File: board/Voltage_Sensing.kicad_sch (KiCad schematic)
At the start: 40 parts, among them U4 Opamp_Dual, U5 Opamp_Dual, U6 Opamp_Dual

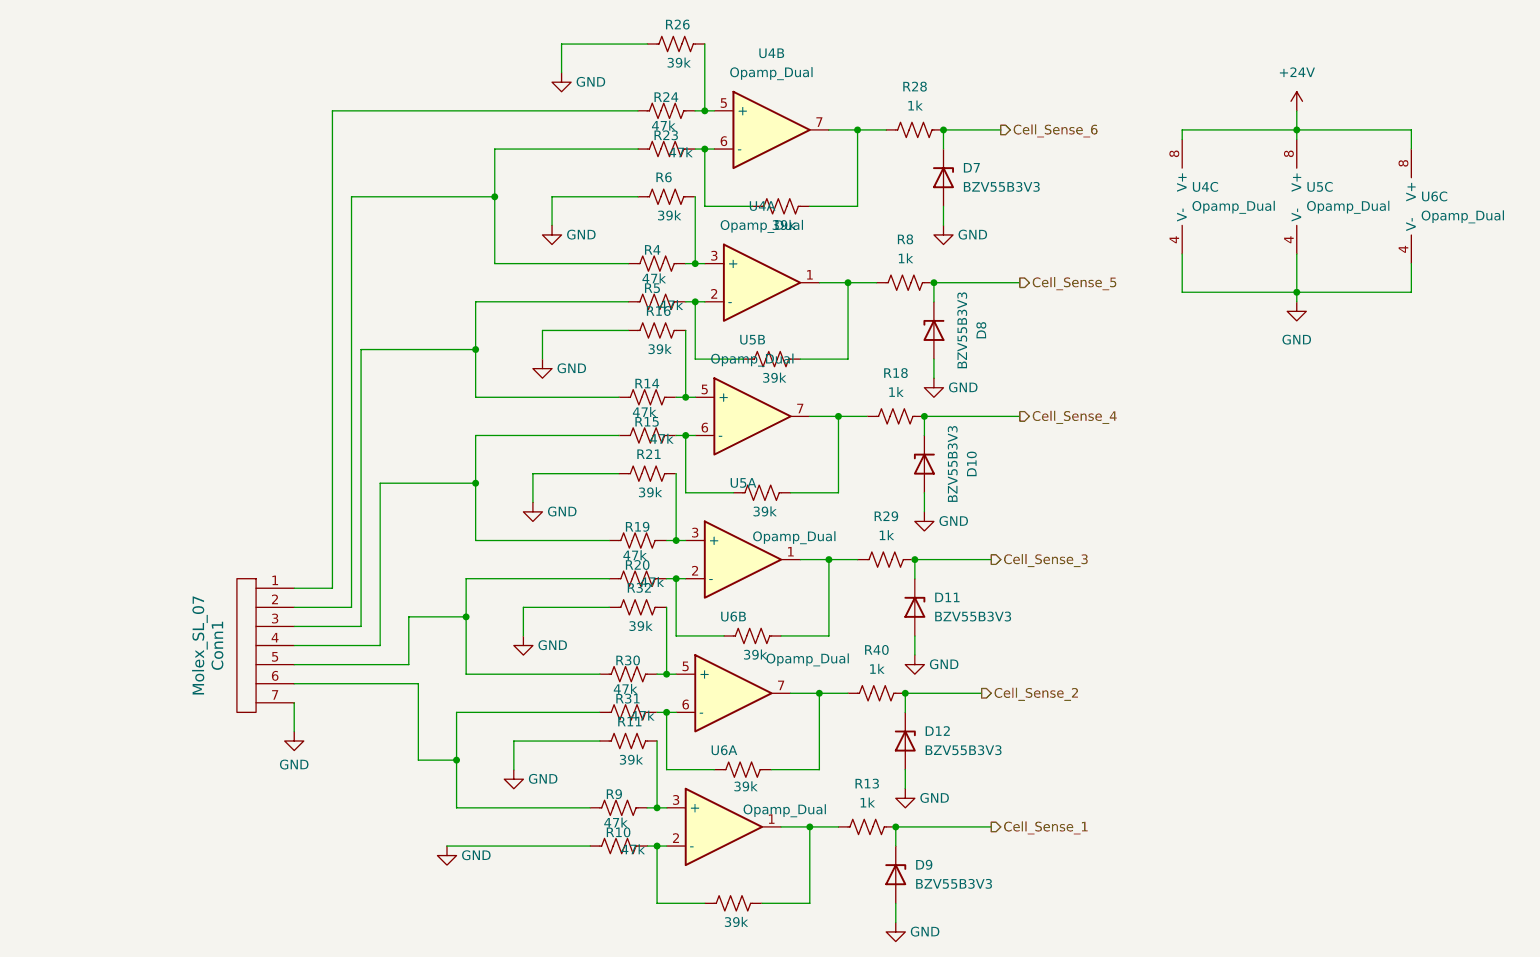
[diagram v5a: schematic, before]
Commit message: Center schematics and layout for prettiness
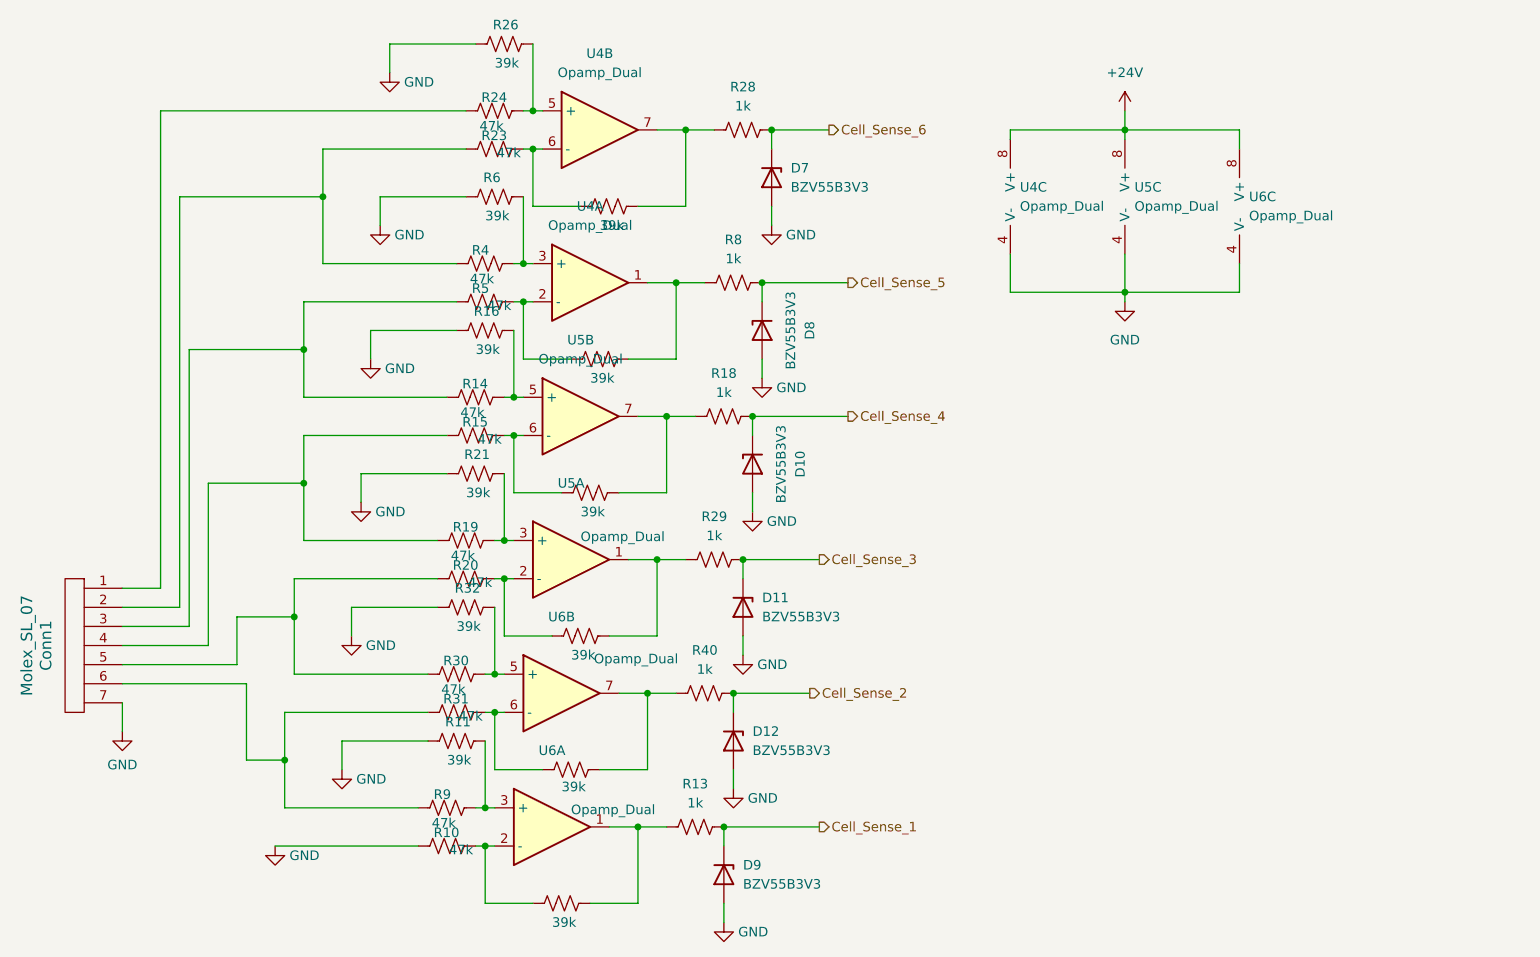
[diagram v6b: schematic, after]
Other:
- moved on the sheet: Conn1, D10, D11, D12, D7, D8, D9, R10, R11, R13, R14, R15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

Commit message: clean up board a tiny bit
this took way too long
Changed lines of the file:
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@@
 		(on_board yes)
 		(dnp no)
-		(fields_autoplaced yes)
 		(property "Reference" "U5"
 			(at 132.08 64.77 0)
@@
 		)
 		(property "Value" "Opamp_Dual"
-			(at 132.08 67.31 0)
+			(at 140.462 71.628 0)
 			(effects
 				(font

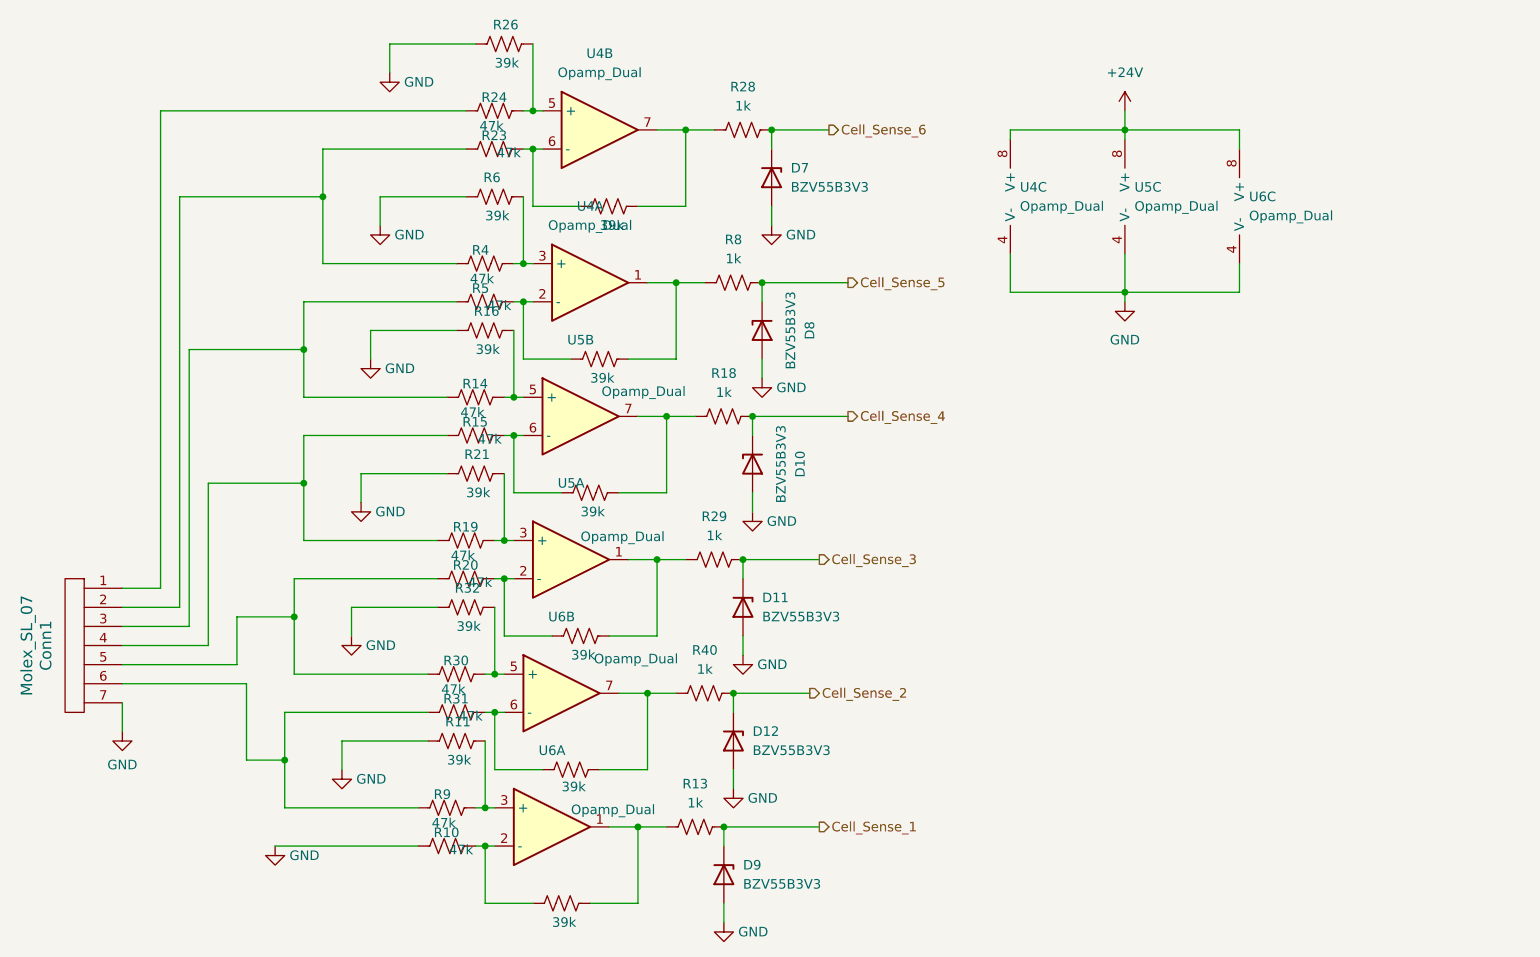
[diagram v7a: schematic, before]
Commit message: add label for battery sensing molex connector
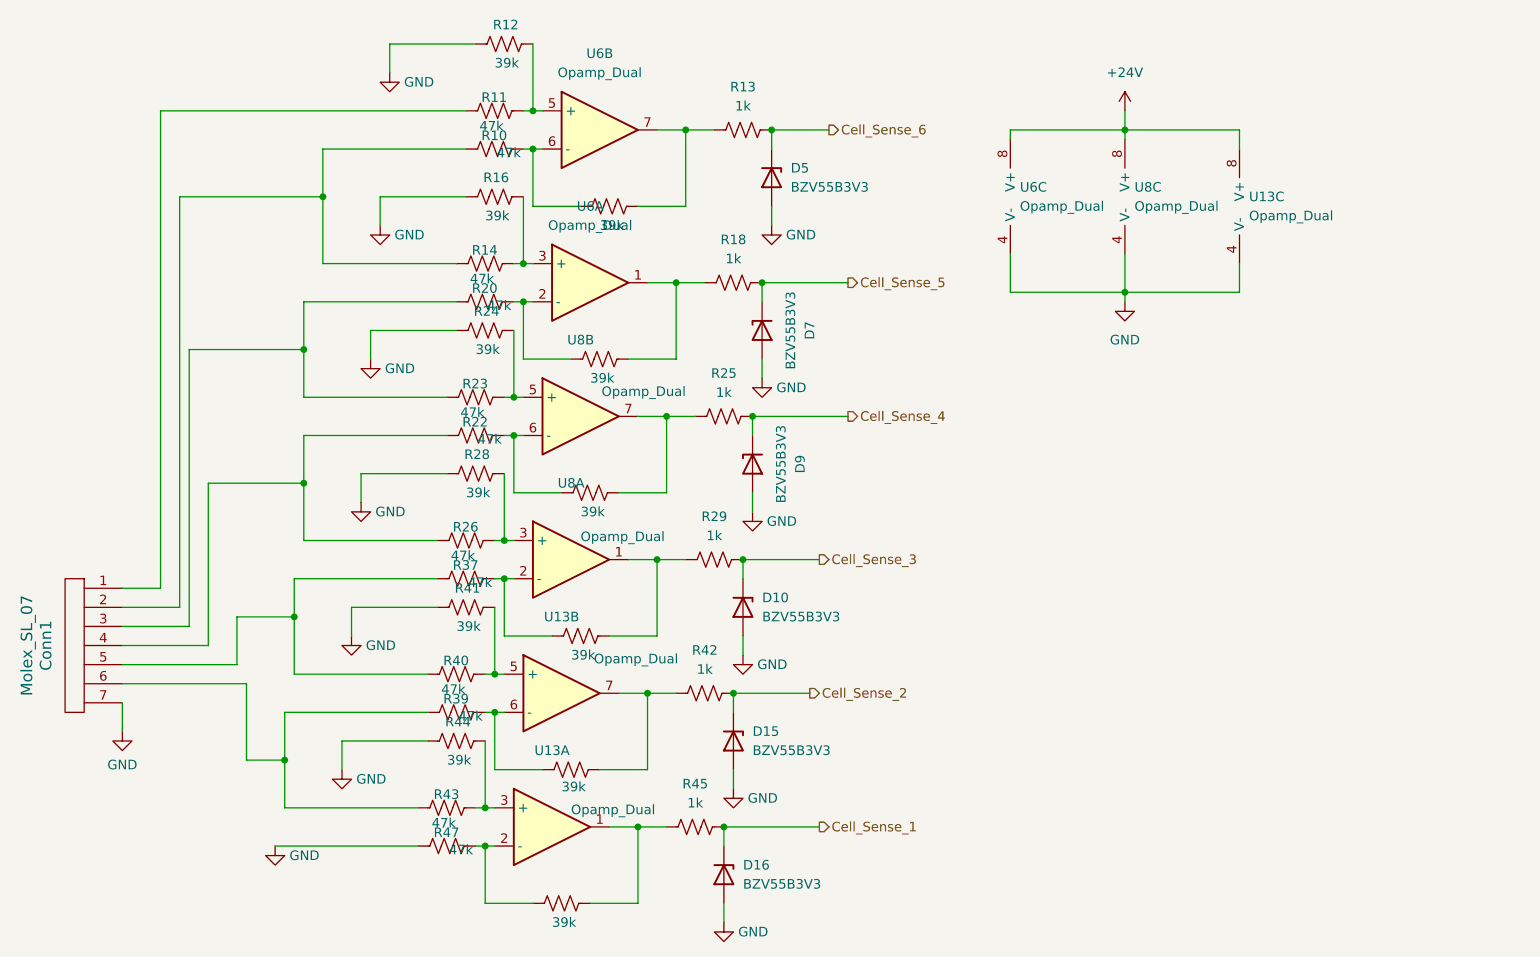
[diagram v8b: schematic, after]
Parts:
- renumbered D11 to D10, D12 to D15, D9 to D16, D7 to D5, D8 to D7, D10 to D9, R23 to R10, R24 to R11, R26 to R12, R28 to R13, R4 to R14, R6 to R16, R8 to R18, R7 to R19, R5 to R20, R17 to R21, R15 to R22, R14 to R23, R16 to R24, R18 to R25, R19 to R26, R21 to R28, R22 to R36, R20 to R37, R33 to R38, R31 to R39, R30 to R40, R32 to R41, R40 to R42, R9 to R43, R11 to R44, R13 to R45, R12 to R46, R10 to R47, R25 to R9, U6 to U13, U4 to U6, U5 to U8
